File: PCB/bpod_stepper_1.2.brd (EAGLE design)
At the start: 83.8 x 62.9 mm, 28 parts, among them IC1 LM3480-5.0, IC2 SN65HVD31DR, J1 282841-4, J8 POWER_JACK

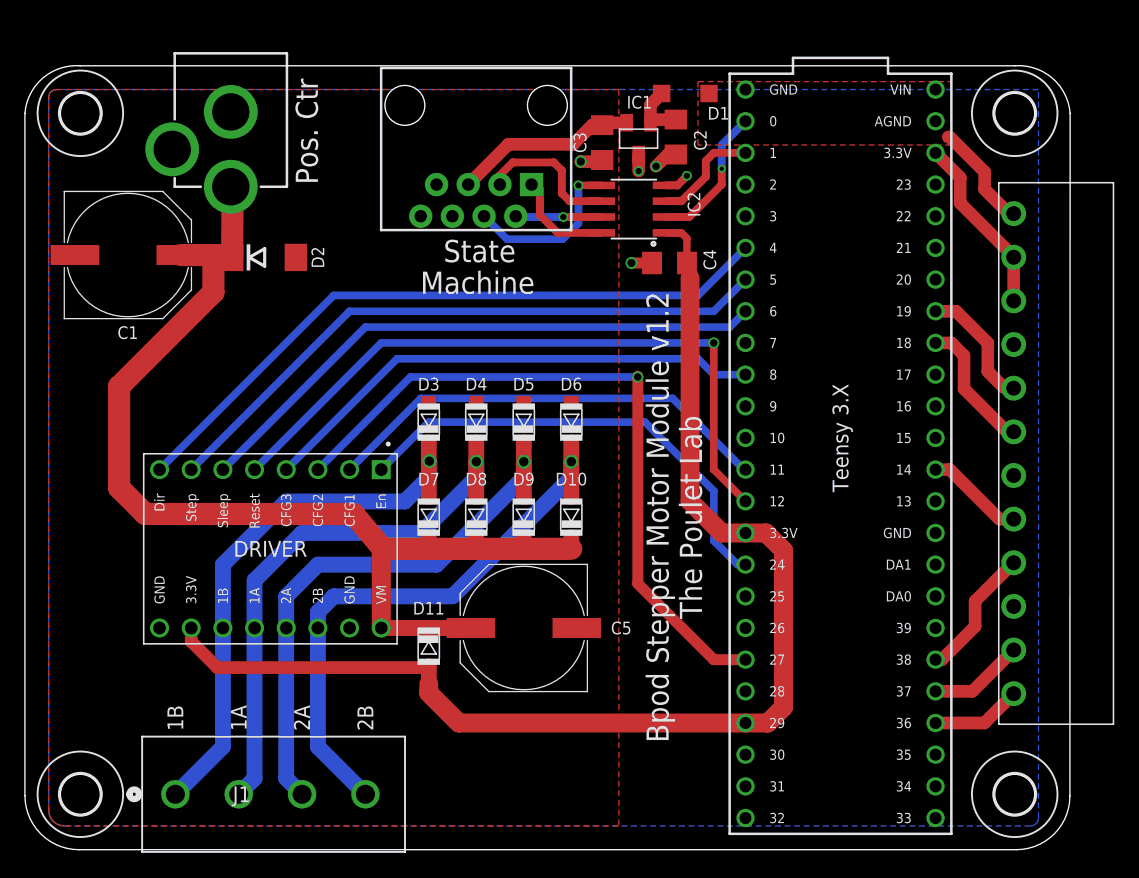
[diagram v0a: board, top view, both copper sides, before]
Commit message: clean-up and minor adjustments
- corrected board dimensions
- clean-up
- resized top ground-plane
- updates to silkscreen
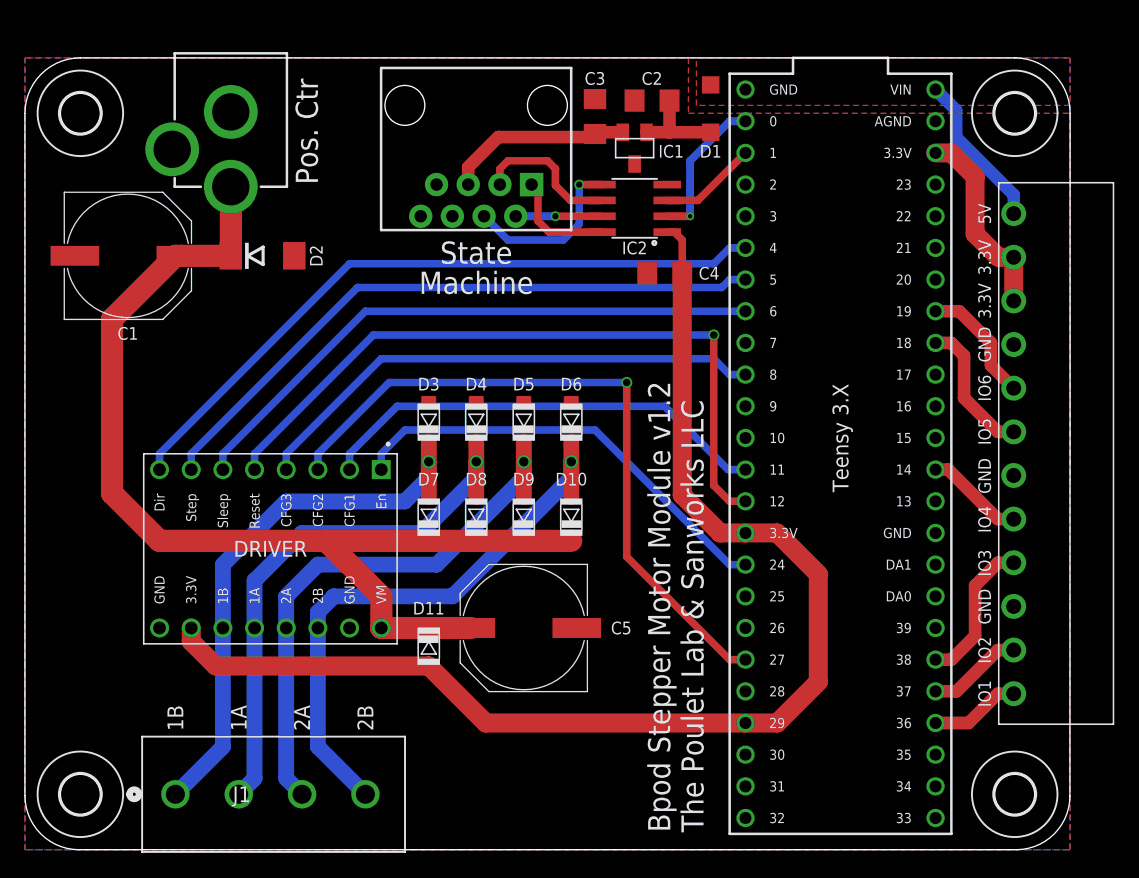
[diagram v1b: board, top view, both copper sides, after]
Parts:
- moved C2 3.49 mm to (50.3, 60.1), turned to 0 degrees
- moved D1 2.36 mm to (55.0, 59.4), turned to 270 degrees
- moved C3 2.17 mm to (45.7, 58.8), turned to 270 degrees
- moved C4 0.91 mm to (51.3, 46.2)
- moved IC1 0.83 mm to (48.9, 56.3)
- moved D2 0.18 mm to (19.1, 47.6)
- moved IC2 0.09 mm to (48.9, 51.4)
- moved C1 0.06 mm to (8.26, 47.6)
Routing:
- net GND: track 8.68 -> 0.00 mm, vias 5 -> 0
- net +5V: track 8.61 -> 12.5 mm
- net 3.3V: track 112.4 -> 115.5 mm
- net N$14: track 4.86 -> 7.69 mm
- net RESET: track 54.8 -> 57.2 mm
- net ENABLE: track 37.9 -> 35.7 mm
- net CFG2: track 56.6 -> 55.3 mm
- net IO3: track 10.7 -> 11.9 mm
- net TX1: track 8.69 -> 7.85 mm
- net SLEEP: track 47.2 -> 47.9 mm
- net STEP: track 50.8 -> 51.5 mm
- net DIRECTION: track 54.4 -> 55.1 mm
- net CFG3: track 41.0 -> 41.8 mm
- net VMOTOR: track 87.6 -> 86.9 mm
- net RX1: track 11.4 -> 12.0 mm
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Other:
- board size 83.8 x 62.9 mm -> 83.8 x 63.5 mm
- board text added: "5V"
- board text added: "Bpod Stepper Motor Module v1.2 The Poulet Lab & Sanworks LLC"
- board text added: "IO1"
- board text added: "IO2"
- board text added: "IO3"
- board text added: "IO4"
- board text added: "IO5"
- board text added: "IO6"
- board text removed: "Bpod Stepper Motor Module v1.2 The Poulet Lab"
